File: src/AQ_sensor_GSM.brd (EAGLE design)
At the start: 110 x 64 mm, 45 parts, among them IC2 MCP73831/OT, J1 F-1X03-SIP-100-32, SW1 PCM12SMTR, SW2 PCM12SMTR, U2 TEXAS_INSTRUMENTS_SN74HC125TE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, U3 TEXAS_INSTRUMENTS_LM1117IMP-3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, X1 53048-08, X2 SIMLOCK-C707_10M006_512_2, X4 50 Ohms

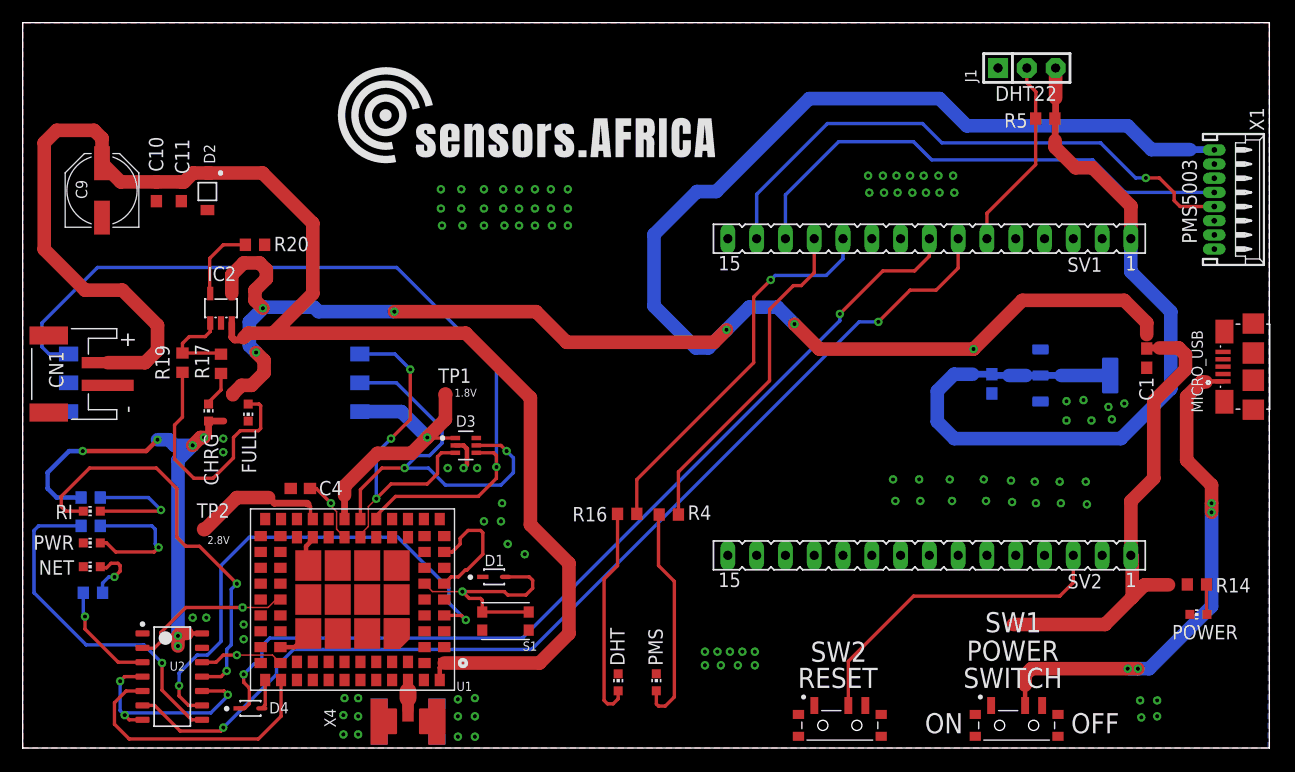
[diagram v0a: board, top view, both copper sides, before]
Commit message: Resolve schematic file error
Schematic file not opening on resolving git merge conflict
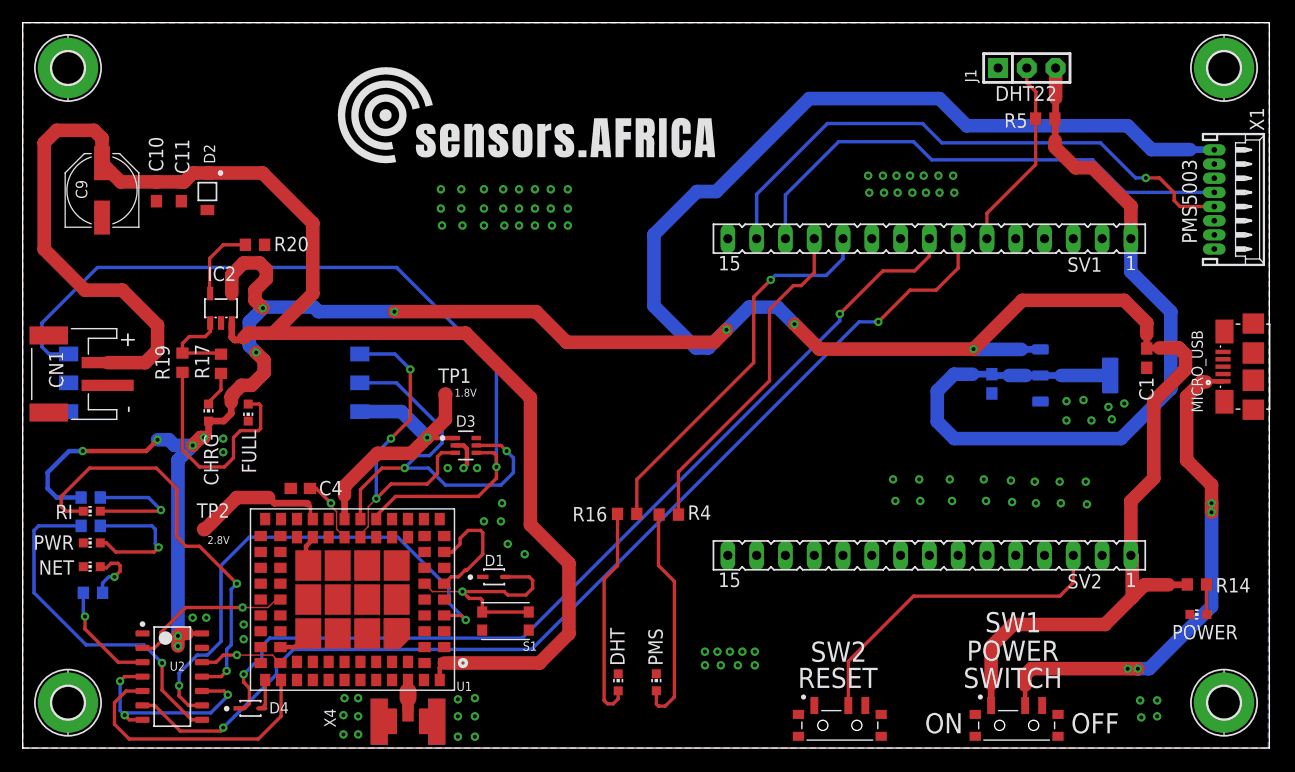
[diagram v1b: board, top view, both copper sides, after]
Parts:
- added H1, H2, H3, H4: MOUNT-PAD-ROUND2.8, AQ_sensor_GSM:2,8-PAD
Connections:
- net GND: now also H1.B2,8, H2.B2,8, H3.B2,8, H4.B2,8
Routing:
- net +5V: track 262.6 -> 283.1 mm
- net N$12: track 22.3 -> 20.0 mm
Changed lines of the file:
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@@
 <attribute name="VALUE" x="87.925" y="33.665" size="1.27" layer="28" rot="MR270"/>
+</element>
+<element name="H1" library="AQ_sensor_GSM" library_urn="urn:adsk.eagle:library:30300195" package="2,8-PAD" package3d_urn="urn:adsk.eagle:package:30300289/1" value="MOUNT-PAD-ROUND2.8" x="106" y="4" smashed="yes">
+<attribute name="POPULARITY" value="6" x="106" y="4" size="1.778" layer="27" display="off"/>
+</element>
+<element name="H2" library="AQ_sensor_GSM" library_urn="urn:adsk.eagle:library:30300195" package="2,8-PAD" package3d_urn="urn:adsk.eagle:package:30300289/1" value="MOUNT-PAD-ROUND2.8" x="106" y="60" smashed="yes">
+<attribute name="POPULARITY" value="6" x="106" y="60" size="1.778" layer="27" display="off"/>
+</element>
+<element name="H3" library="AQ_sensor_GSM" library_urn="urn:adsk.eagle:library:30300195" package="2,8-PAD" package3d_urn="urn:adsk.eagle:package:30300289/1" value="MOUNT-PAD-ROUND2.8" x="4" y="60" smashed="yes">
+<attribute name="POPULARITY" value="6" x="4" y="60" size="1.778" layer="27" display="off"/>
+</element>
+<element name="H4" library="AQ_sensor_GSM" library_urn="urn:adsk.eagle:library:30300195" package="2,8-PAD" package3d_urn="urn:adsk.eagle:package:30300289/1" value="MOUNT-PAD-ROUND2.8" x="4" y="4" smashed="yes">
+<attribute name="POPULARITY" value="6" x="4" y="4" size="1.778" layer="27" display="off"/>
 </element>
 <element name="DHT" library="led" library_urn="urn:adsk.eagle:library:259" package="CHIP-LED0603" package3d_urn="urn:adsk.eagle:package:15819/3" value="GREEN" x="52.54416875" y="5.7942" smashed="yes">
@@
 <contactref element="X1" pad="7"/>
 <contactref element="C1" pad="2"/>
+<contactref element="H1" pad="B2,8"/>
+<contactref element="H2" pad="B2,8"/>
+<contactref element="H3" pad="B2,8"/>
+<contactref element="H4" pad="B2,8"/>
 <contactref element="SV2" pad="2"/>
 <contactref element="DHT" pad="C"/>
@@
 <via x="21.2" y="38.8" extent="1-16" drill="0.35"/>
 <via x="20.6" y="34.9" extent="1-16" drill="0.35"/>
+<wire x1="102.51" y1="14.18" x2="102.76" y2="14.43" width="0.4" layer="1"/>
 <via x="32.8" y="38.5" extent="1-16" drill="0.35"/>
 <via x="62.1" y="36.9" extent="1-16" drill="0.35"/>
+<wire x1="89.775" y1="35.2" x2="89.805" y2="35.17" width="0.4" layer="16"/>
 <contactref element="U2" pad="14"/>
 <wire x1="14.51" y1="10.11" x2="15.825" y2="10.11" width="0.4" layer="1"/>
@@
 <wire x1="3" y1="22.1" x2="5.15" y2="22.1" width="0.4" layer="16"/>
 <wire x1="4.1" y1="26.2" x2="2.2" y2="24.3" width="0.4" layer="16"/>
+<wire x1="85.45" y1="3.75" x2="85.45" y2="5.65" width="0.6" layer="1"/>
+<wire x1="85.5" y1="5.7" x2="85.45" y2="5.65" width="0.6" layer="1"/>
+<wire x1="85.45" y1="5.65" x2="85.45" y2="8.95" width="1.2" layer="1"/>
 <wire x1="95.5" y1="10.9" x2="97.9" y2="13.3" width="1.2" layer="1"/>
 <wire x1="97.9" y1="13.3" x2="97.9" y2="16.88" width="1.2" layer="1"/>
 <wire x1="97.9" y1="16.88" x2="97.78" y2="17" width="1.2" layer="1"/>
-<wire x1="95.5" y1="10.9" x2="87.4" y2="10.9" width="1.2" layer="1"/>
-<wire x1="99" y1="14.4" x2="101.1" y2="14.4" width="1.2" layer="1"/>
+<wire x1="85.45" y1="8.95" x2="87.4" y2="10.9" width="1.2" layer="1"/>
+<wire x1="87.4" y1="10.9" x2="95.5" y2="10.9" width="1.2" layer="1"/>
+<wire x1="102.76" y1="14.43" x2="102.73" y2="14.4" width="0.6" layer="1"/>
+<wire x1="102.73" y1="14.4" x2="101.1" y2="14.4" width="0.6" layer="1"/>
+<wire x1="101.1" y1="14.4" x2="99" y2="14.4" width="1.2" layer="1"/>
 <wire x1="99" y1="14.4" x2="97.9" y2="13.3" width="1.2" layer="1"/>
 <wire x1="97.78" y1="17" x2="97.78" y2="21.78" width="1.2" layer="1"/>
@@
 <wire x1="102.6" y1="34.7" x2="102" y2="35.3" width="1.2" layer="1"/>
 <wire x1="102" y1="35.3" x2="100.3" y2="35.3" width="1.2" layer="1"/>
-<wire x1="99.18" y1="37.52" x2="99.18" y2="36.48" width="1.2" layer="1"/>
+<wire x1="99.18" y1="35.25" x2="99.18" y2="36.48" width="0.6" layer="1"/>
+<wire x1="99.18" y1="36.48" x2="99.2" y2="36.5" width="0.6" layer="1"/>
+<wire x1="99.18" y1="36.48" x2="99.18" y2="37.52" width="1.2" layer="1"/>
+<wire x1="89.805" y1="35.17" x2="88.13" y2="35.17" width="0.6" layer="16"/>
+<wire x1="88.13" y1="35.17" x2="88.1" y2="35.2" width="0.6" layer="16"/>
+<wire x1="88.13" y1="35.17" x2="83.93" y2="35.17" width="1.2" layer="16"/>
+<wire x1="83.93" y1="35.17" x2="83.9" y2="35.2" width="1.2" layer="16"/>
 <via x="83.9" y="35.2" extent="1-16" drill="0.35"/>
 <wire x1="83.9" y1="35.2" x2="70.3" y2="35.2" width="1.2" layer="1"/>
@@
 <wire x1="21.3" y1="33.1" x2="20.2" y2="32" width="1.2" layer="1"/>
 <wire x1="18.55" y1="31.25" x2="18.55" y2="31.165075" width="1.2" layer="1"/>
+<wire x1="18.55" y1="31.165075" x2="18.4" y2="31.015075" width="1.2" layer="1"/>
+<wire x1="18.4" y1="31.015075" x2="18.4" y2="30.5" width="1.2" layer="1"/>
 <wire x1="20.2" y1="32" x2="19.3" y2="32" width="1.2" layer="1"/>
 <wire x1="19.3" y1="32" x2="18.55" y2="31.25" width="1.2" layer="1"/>
+<wire x1="18.4" y1="29.5" x2="18.4" y2="31.015075" width="0.6" layer="1"/>
 <wire x1="16.4" y1="28.85" x2="17.75" y2="28.85" width="0.6" layer="1"/>
+<wire x1="17.75" y1="28.85" x2="18.4" y2="29.5" width="0.6" layer="1"/>
 <wire x1="99.18" y1="37.52" x2="97.2" y2="39.5" width="1.2" layer="1"/>
 <wire x1="88.2" y1="39.5" x2="83.9" y2="35.2" width="1.2" layer="1"/>
@@
 <wire x1="25.2" y1="21.5" x2="25.1" y2="21.6" width="0.6" layer="1"/>
 <wire x1="25.1" y1="21.6" x2="22.2" y2="21.6" width="0.6" layer="1"/>
-<wire x1="21.7" y1="22.1" x2="22.2" y2="21.6" width="0.6" layer="1"/>
-<wire x1="16.1" y1="19.3" x2="18.9" y2="22.1" width="1.2" layer="1"/>
-<wire x1="18.9" y1="22.1" x2="21.7" y2="22.1" width="1.2" layer="1"/>
+<wire x1="22.2" y1="21.6" x2="21.7" y2="22.1" width="0.6" layer="1"/>
+<wire x1="18.9" y1="22.1" x2="16.1" y2="19.3" width="1.2" layer="1"/>
+<wire x1="21.7" y1="22.1" x2="18.9" y2="22.1" width="1.2" layer="1"/>
 </signal>
 <signal name="PWRKEY" class="2">
@@
 <wire x1="37.3" y1="31.2" x2="37.3" y2="29" width="1.2" layer="1"/>
 <wire x1="35.75" y1="27.35" x2="35.7" y2="27.4" width="0.6" layer="1"/>
-<wire x1="38.175" y1="27.35" x2="35.75" y2="27.35" width="0.3" layer="1"/>
+<wire x1="38.175" y1="27.35" x2="35.75" y2="27.35" width="0.4" layer="1"/>
 </signal>
 <signal name="SIMDATA">
@@
 <wire x1="34.8" y1="25.8" x2="35.9" y2="25.8" width="0.3" layer="16"/>
 <wire x1="35.9" y1="25.8" x2="37" y2="26.9" width="0.3" layer="16"/>
+<wire x1="37" y1="26.9" x2="37" y2="28.2" width="0.3" layer="16"/>
 <wire x1="37" y1="28.2" x2="32.975" y2="32.225" width="0.3" layer="16"/>
 <wire x1="32.975" y1="32.225" x2="29.75" y2="32.225" width="0.3" layer="16"/>
@@
 <wire x1="35.8" y1="24.7" x2="37.3" y2="23.2" width="0.3" layer="16"/>
 <wire x1="37.3" y1="23.2" x2="42.2" y2="23.2" width="0.3" layer="16"/>
-<wire x1="37" y1="26.9" x2="37" y2="28.2" width="0.3" layer="16"/>
 </signal>
 <signal name="GSM_ANT">
@@
 <contactref element="FULL" pad="A"/>
 <contactref element="R19" pad="1"/>
-<wire x1="18.6" y1="25.6" x2="18.6" y2="27.4" width="0.3" layer="1"/>
+<wire x1="15.6" y1="24.8" x2="17.8" y2="24.8" width="0.3" layer="1"/>
+<wire x1="17.8" y1="24.8" x2="18.6" y2="25.6" width="0.3" layer="1"/>
+<wire x1="14.1" y1="33.15" x2="14.1" y2="26.3" width="0.3" layer="1"/>
+<wire x1="14.1" y1="26.3" x2="15.6" y2="24.8" width="0.3" layer="1"/>
+<wire x1="18.6" y1="27.4" x2="18.6" y2="25.6" width="0.3" layer="1"/>
 <wire x1="19.9" y1="30.35" x2="20.85" y2="30.35" width="0.3" layer="1"/>
 <wire x1="20.85" y1="30.35" x2="21" y2="30.2" width="0.3" layer="1"/>
@@
 <wire x1="21" y1="28.2" x2="20.8" y2="28" width="0.3" layer="1"/>
 <wire x1="20.8" y1="28" x2="19.2" y2="28" width="0.3" layer="1"/>
-<wire x1="14.1" y1="33.15" x2="14.1" y2="29.2" width="0.3" layer="1"/>
-<wire x1="14.1" y1="29.2" x2="13.4" y2="28.5" width="0.3" layer="1"/>
-<wire x1="13.4" y1="28.5" x2="13.4" y2="25.5" width="0.3" layer="1"/>
-<wire x1="13.4" y1="25.5" x2="15.1" y2="23.8" width="0.3" layer="1"/>
-<wire x1="15.1" y1="23.8" x2="16.8" y2="23.8" width="0.3" layer="1"/>
-<wire x1="16.8" y1="23.8" x2="18.6" y2="25.6" width="0.3" layer="1"/>
 </signal>
 <signal name="N$13">
@@
 <mfgpreviewcolors>
 <mfgpreviewcolor name="soldermaskcolor" color="0xC8008000"/>
-<mfgpreviewcolor name="silkscreencolor" color="0xFFFFFFFF"/>
+<mfgpreviewcolor name="silkscreencolor" color="0xFFFEFEFE"/>
 <mfgpreviewcolor name="backgroundcolor" color="0xFF282828"/>
 <mfgpreviewcolor name="coppercolor" color="0xFFFFBF00"/>
@@
 </note>
 <note version="8.3" severity="warning">
-Since Version 8.3, EAGLE supports Fusion synchronisation.
-This feature will not be available in this version and saving
-the document will break the link to the Fusion PCB feature.
-</note>
-<note version="8.3" severity="warning">

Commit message: Ripup
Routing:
- net +5V: track 283.1 -> 0.00 mm, vias 12 -> 0
- net V_LIPO: track 136.5 -> 0.00 mm
- net GSM_TX_5V: track 92.9 -> 0.00 mm, vias 2 -> 0
- net GSM_RX_O: track 82.4 -> 0.00 mm, vias 2 -> 0
- net SIMDATA: track 75.4 -> 0.00 mm, vias 1 -> 0
- net +3V3: track 75.1 -> 0.00 mm
- net PMS_TX: track 50.3 -> 0.00 mm, vias 1 -> 0
- net VIN: track 46.5 -> 0.00 mm, vias 4 -> 0
- net PMS_RX: track 45.5 -> 0.00 mm
- net PWRSTAT: track 44.4 -> 0.00 mm, vias 2 -> 0
- net GND: track 39.1 -> 0.00 mm, vias 103 -> 0
- net SIMRST: track 37.4 -> 0.00 mm, vias 2 -> 0
- net RI_5V: track 36.7 -> 0.00 mm, vias 2 -> 0
- net DHT_LED: track 34.5 -> 0.00 mm, vias 1 -> 0
- net SIMCLK: track 31.2 -> 0.00 mm, vias 3 -> 0
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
